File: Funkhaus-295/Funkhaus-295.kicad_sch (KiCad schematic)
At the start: 86 parts, among them SW1 SW_DPDT_x2, SW2 SW_Rotary3x4, SW3 SW_Rotary2x6, U1 TL074, U2 TL074, U3 TL074

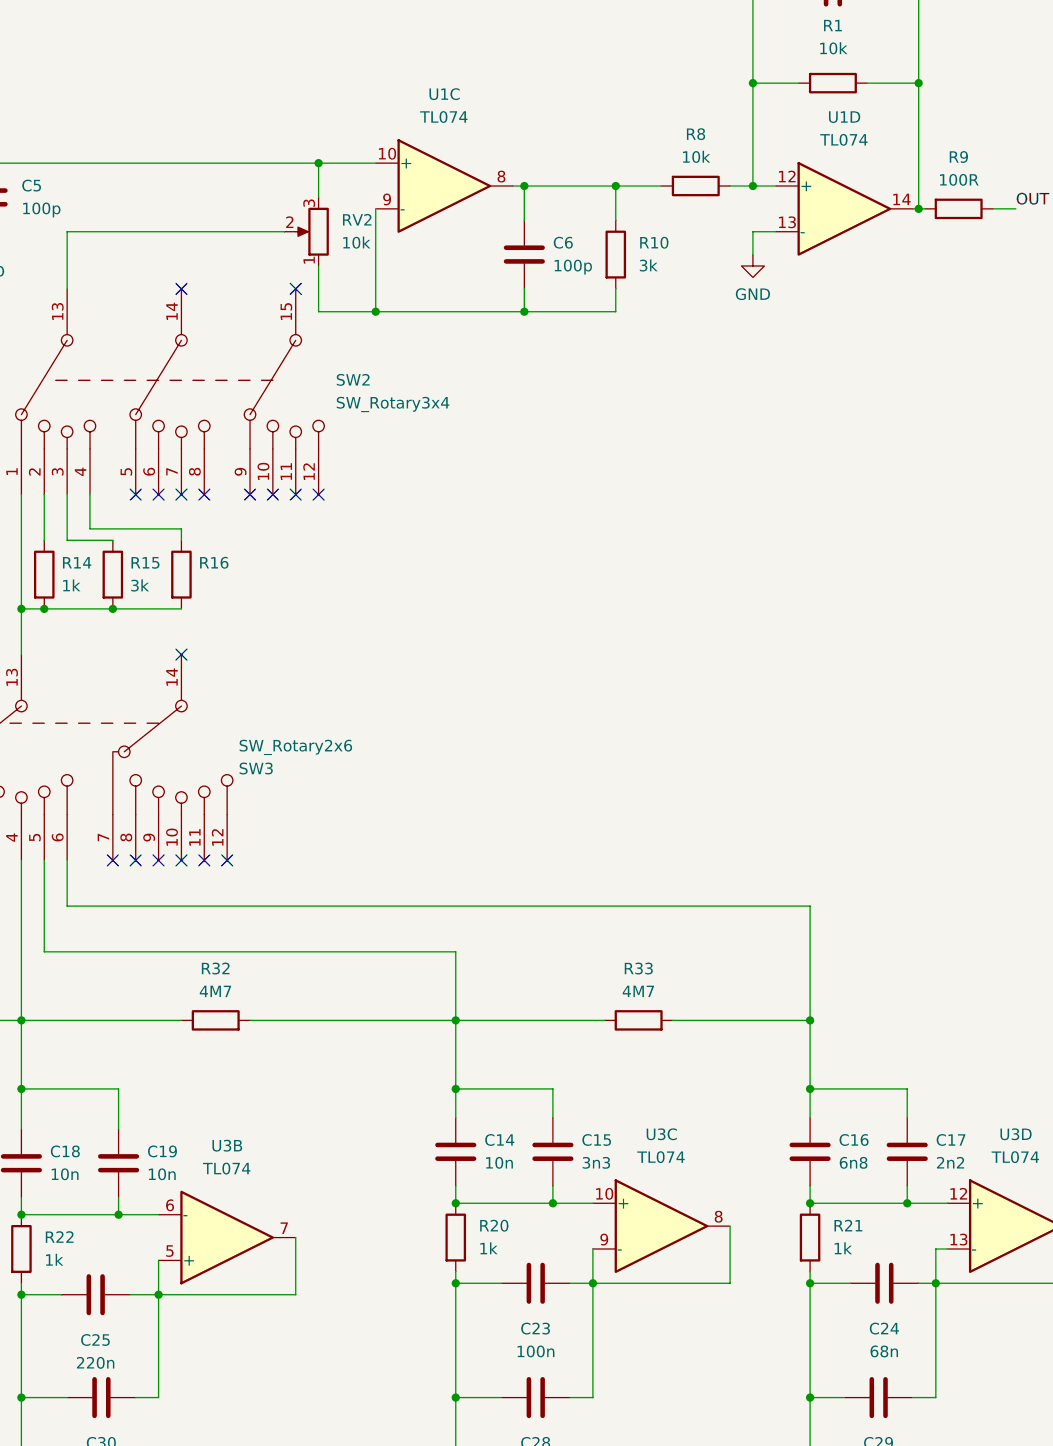
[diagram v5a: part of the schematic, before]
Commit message: Rev 05c
corrected the orientation of several opamps
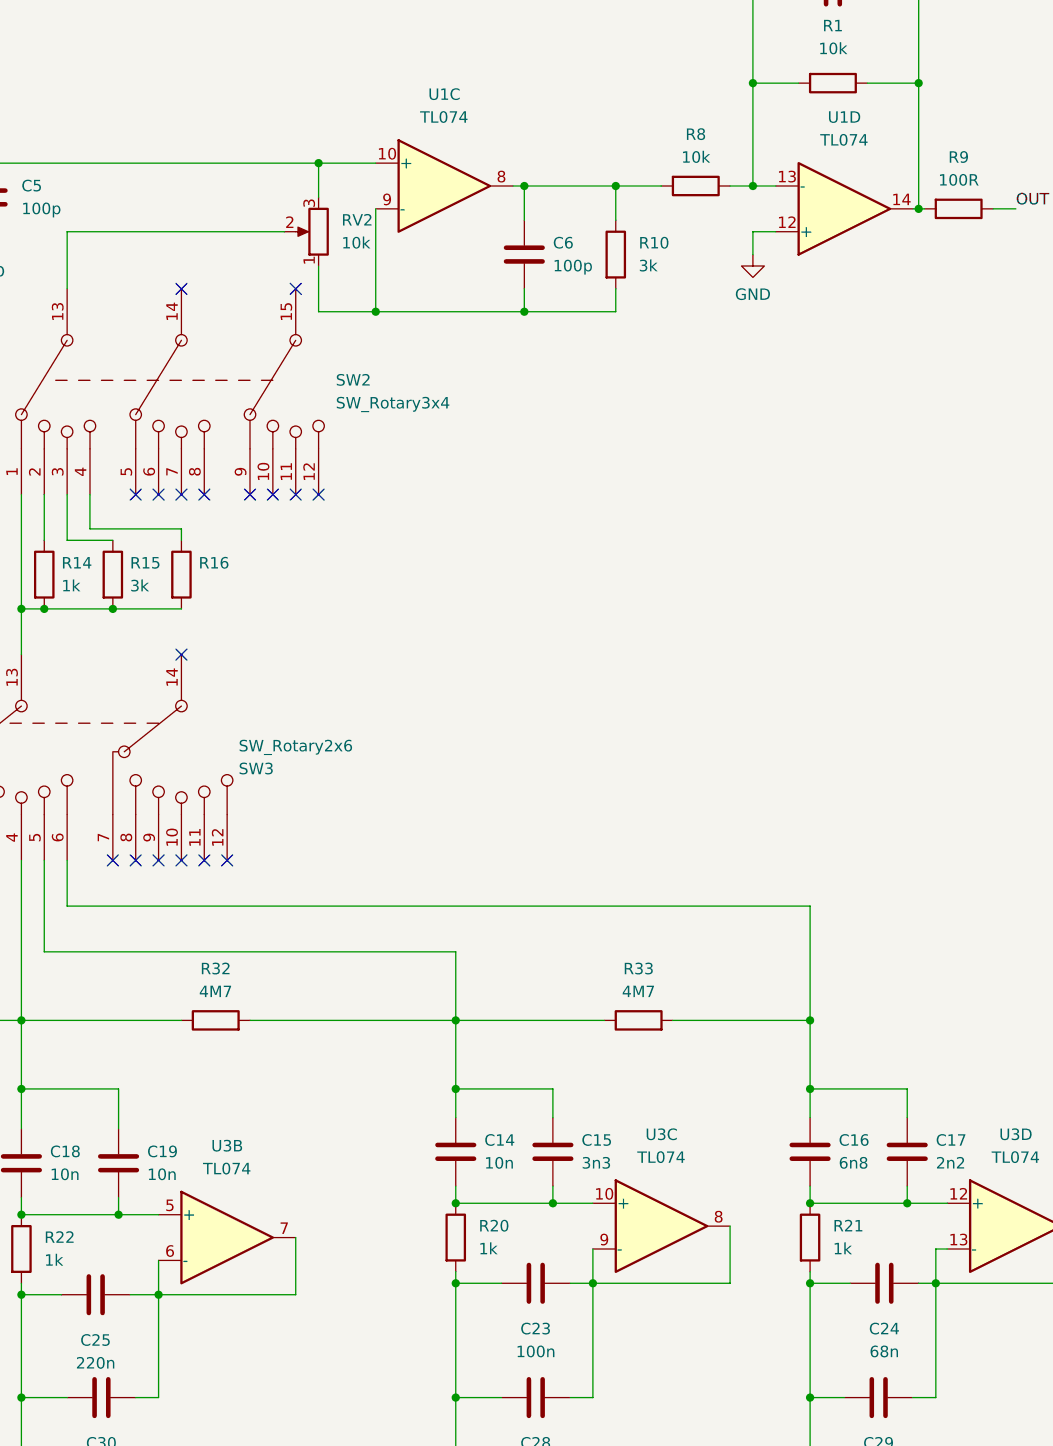
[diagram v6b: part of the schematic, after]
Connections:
- net GND: now also U1.12 (+); no longer U1.13 (-)
- net at C25.2, C30.2, U3.7: now also U3.6 (-); no longer U3.5 (+)
- net at C18.2, C19.2, R22.1: now also U3.5 (+); no longer U3.6 (-)
- net at C1.1, R1.2, R8.1: now also U1.13 (-); no longer U1.12 (+)
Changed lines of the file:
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@@
   (title_block
     (title "SIAM 295b")
-    (date "2022-08-07")
-    (rev "05a")
+    (date "2022-08-08")
+    (rev "05b")
     (company "Robert-André Vettel")
     (comment 1 "Siemens Inspired Audio Module")
@@
     (pin "2")
   )
-  (symbol (lib_id "Amplifier_Operational:TL074") (at 360.68 58.42 0) (unit 4)
+  (symbol (lib_id "Amplifier_Operational:TL074") (at 360.68 58.42 0) (mirror x) (unit 4)
     (in_bom yes) (on_board yes) (fields_autoplaced)
     (property "Reference" "U1" (id 0) (at 360.68 48.26 0))
     (property "Value" "TL074" (id 1) (at 360.68 50.8 0))
-    (property "Footprint" "" (id 2) (at 359.41 55.88 0)
-      (effects (font (size 1.27 1.27)) hide)
-    )
-    (property "Datasheet" "http://www.ti.com/lit/ds/symlink/tl071.pdf" (id 3) (at 361.95 53.34 0)
+    (property "Footprint" "" (id 2) (at 359.41 60.96 0)
+      (effects (font (size 1.27 1.27)) hide)
+    )
+    (property "Datasheet" "http://www.ti.com/lit/ds/symlink/tl071.pdf" (id 3) (at 361.95 63.5 0)
       (effects (font (size 1.27 1.27)) hide)
     )
@@
     (pin "1")
   )
-  (symbol (lib_id "Amplifier_Operational:TL074") (at 292.1 172.72 0) (mirror x) (unit 2)
+  (symbol (lib_id "Amplifier_Operational:TL074") (at 292.1 172.72 0) (unit 2)
     (in_bom yes) (on_board yes) (fields_autoplaced)
     (property "Reference" "U3" (id 0) (at 292.1 162.56 0))
     (property "Value" "TL074" (id 1) (at 292.1 165.1 0))
-    (property "Footprint" "" (id 2) (at 290.83 175.26 0)
-      (effects (font (size 1.27 1.27)) hide)
-    )
-    (property "Datasheet" "http://www.ti.com/lit/ds/symlink/tl071.pdf" (id 3) (at 293.37 177.8 0)
-      (effects (font (size 1.27 1.27)) hide)
-    )
+    (property "Footprint" "" (id 2) (at 290.83 170.18 0)
+      (effects (font (size 1.27 1.27)) hide)
+    )
+    (property "Datasheet" "http://www.ti.com/lit/ds/symlink/tl071.pdf" (id 3) (at 293.37 167.64 0)
+      (effects (font (size 1.27 1.27)) hide)
+    )

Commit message: housekeeping (Rev05C)
- corrected missing 10K resistor
- added output capacitor
- added annotations
- changed component numbering to make a little more sense
- added partial component footprints
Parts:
- added C34: 22u, Capacitor_THT:CP_Radial_D5.0mm_P2.50mm, symbol Device:C_Polarized
- added R32, R33, R34, R35, R36, R37, R38: 4M7, Resistor_THT:R_Axial_DIN0207_L6.3mm_D2.5mm_P2.54mm_Vertical, symbol Device:R
- C1: renamed from C8; footprint Capacitor_THT:C_Rect_L10.0mm_W3.0mm_P7.50mm_MKS4 -> (none)
- C2: renamed from C4; footprint Capacitor_THT:C_Rect_L10.0mm_W3.0mm_P7.50mm_MKS4 -> (none)
- C28: renamed from C5; footprint (none) -> Capacitor_THT:C_Disc_D5.0mm_W2.5mm_P5.00mm
- C29: renamed from C6; footprint (none) -> Capacitor_THT:C_Disc_D5.0mm_W2.5mm_P5.00mm
- C3: renamed from C9; footprint Capacitor_THT:C_Rect_L10.0mm_W3.0mm_P7.50mm_MKS4 -> (none)
- C31: renamed from C1; footprint (none) -> Capacitor_THT:C_Disc_D5.0mm_W2.5mm_P5.00mm
- C32: renamed from C2; footprint (none) -> Capacitor_THT:CP_Radial_D10.0mm_P5.00mm
- C33: renamed from C3; footprint (none) -> Capacitor_THT:CP_Radial_D5.0mm_P2.50mm
- C35: renamed from C31; footprint (none) -> Capacitor_THT:CP_Radial_D10.0mm_P5.00mm
- C36: renamed from C34; footprint (none) -> Capacitor_THT:CP_Radial_D10.0mm_P5.00mm
- C37: renamed from C32; footprint Capacitor_THT:C_Rect_L10.0mm_W3.0mm_P7.50mm_MKS4 -> Capacitor_THT:C_Disc_D5.0mm_W2.5mm_P5.00mm
- C38: renamed from C33; footprint Capacitor_THT:C_Rect_L10.0mm_W3.0mm_P7.50mm_MKS4 -> Capacitor_THT:C_Disc_D5.0mm_W2.5mm_P5.00mm
- C39: renamed from C35; footprint Capacitor_THT:C_Rect_L10.0mm_W3.0mm_P7.50mm_MKS4 -> Capacitor_THT:C_Disc_D5.0mm_W2.5mm_P5.00mm
- C40: renamed from C36; footprint Capacitor_THT:C_Rect_L10.0mm_W3.0mm_P7.50mm_MKS4 -> Capacitor_THT:C_Disc_D5.0mm_W2.5mm_P5.00mm
- C41: renamed from C37; footprint Capacitor_THT:C_Rect_L10.0mm_W3.0mm_P7.50mm_MKS4 -> Capacitor_THT:C_Disc_D5.0mm_W2.5mm_P5.00mm
- C42: renamed from C38; footprint Capacitor_THT:C_Rect_L10.0mm_W3.0mm_P7.50mm_MKS4 -> Capacitor_THT:C_Disc_D5.0mm_W2.5mm_P5.00mm
- R10: renamed from R34; footprint (none) -> Resistor_THT:R_Axial_DIN0207_L6.3mm_D2.5mm_P10.16mm_Horizontal
- R11: renamed from R17; footprint (none) -> Resistor_THT:R_Axial_DIN0207_L6.3mm_D2.5mm_P10.16mm_Horizontal
- R12: renamed from R24; footprint (none) -> Resistor_THT:R_Axial_DIN0207_L6.3mm_D2.5mm_P10.16mm_Horizontal
- R13: renamed from R35; footprint (none) -> Resistor_THT:R_Axial_DIN0207_L6.3mm_D2.5mm_P10.16mm_Horizontal
- R14: renamed from R36; footprint (none) -> Resistor_THT:R_Axial_DIN0207_L6.3mm_D2.5mm_P10.16mm_Horizontal
- R15: renamed from R18; footprint (none) -> Resistor_THT:R_Axial_DIN0207_L6.3mm_D2.5mm_P10.16mm_Horizontal
- R16: renamed from R23; footprint (none) -> Resistor_THT:R_Axial_DIN0207_L6.3mm_D2.5mm_P10.16mm_Horizontal
- R17: renamed from R7; footprint (none) -> Resistor_THT:R_Axial_DIN0207_L6.3mm_D2.5mm_P10.16mm_Horizontal
- R18: renamed from R22; footprint (none) -> Resistor_THT:R_Axial_DIN0207_L6.3mm_D2.5mm_P10.16mm_Horizontal
- R19: renamed from R28; footprint (none) -> Resistor_THT:R_Axial_DIN0207_L6.3mm_D2.5mm_P10.16mm_Horizontal
- R20: renamed from R14; footprint (none) -> Resistor_THT:R_Axial_DIN0207_L6.3mm_D2.5mm_P10.16mm_Horizontal
- R21: renamed from R15; footprint (none) -> Resistor_THT:R_Axial_DIN0207_L6.3mm_D2.5mm_P10.16mm_Horizontal
- R22: renamed from R16; value ~ -> 10k; footprint (none) -> Resistor_THT:R_Axial_DIN0207_L6.3mm_D2.5mm_P10.16mm_Horizontal
- R23: renamed from R20; footprint (none) -> Resistor_THT:R_Axial_DIN0207_L6.3mm_D2.5mm_P10.16mm_Horizontal
- R24: renamed from R26; footprint (none) -> Resistor_THT:R_Axial_DIN0207_L6.3mm_D2.5mm_P10.16mm_Horizontal
- R25: renamed from R10; footprint (none) -> Resistor_THT:R_Axial_DIN0207_L6.3mm_D2.5mm_P10.16mm_Horizontal
- R26: renamed from R21; footprint (none) -> Resistor_THT:R_Axial_DIN0207_L6.3mm_D2.5mm_P10.16mm_Horizontal
- R27: footprint (none) -> Resistor_THT:R_Axial_DIN0207_L6.3mm_D2.5mm_P10.16mm_Horizontal
- R28: renamed from R6; footprint (none) -> Resistor_THT:R_Axial_DIN0207_L6.3mm_D2.5mm_P10.16mm_Horizontal
- R29: renamed from R8; footprint (none) -> Resistor_THT:R_Axial_DIN0207_L6.3mm_D2.5mm_P10.16mm_Horizontal
- R30: renamed from R1; footprint (none) -> Resistor_THT:R_Axial_DIN0207_L6.3mm_D2.5mm_P10.16mm_Horizontal
- R31: renamed from R9; footprint (none) -> Resistor_THT:R_Axial_DIN0207_L6.3mm_D2.5mm_P10.16mm_Horizontal
- R39: renamed from R29; footprint (none) -> Resistor_THT:R_Axial_DIN0207_L6.3mm_D2.5mm_P2.54mm_Vertical
- R40: renamed from R30; footprint (none) -> Resistor_THT:R_Axial_DIN0207_L6.3mm_D2.5mm_P2.54mm_Vertical
- R41: renamed from R31; footprint (none) -> Resistor_THT:R_Axial_DIN0207_L6.3mm_D2.5mm_P2.54mm_Vertical
- R42: renamed from R32; footprint (none) -> Resistor_THT:R_Axial_DIN0207_L6.3mm_D2.5mm_P2.54mm_Vertical
- R43: renamed from R33; footprint (none) -> Resistor_THT:R_Axial_DIN0207_L6.3mm_D2.5mm_P2.54mm_Vertical
- R8: renamed from R19; footprint (none) -> Resistor_THT:R_Axial_DIN0207_L6.3mm_D2.5mm_P10.16mm_Horizontal
- R9: renamed from R25; footprint (none) -> Resistor_THT:R_Axial_DIN0207_L6.3mm_D2.5mm_P10.16mm_Horizontal
- RV1, RV2, RV3: footprint (none) -> Connector_PinHeader_2.54mm:PinHeader_1x03_P2.54mm_Horizontal
- SW1: footprint (none) -> Connector_PinHeader_2.54mm:PinHeader_2x03_P2.54mm_Horizontal
- SW2: footprint (none) -> Connector_PinHeader_2.54mm:PinHeader_1x05_P2.54mm_Horizontal
- SW3: footprint (none) -> Connector_PinHeader_2.54mm:PinHeader_1x07_P2.54mm_Horizontal
- U1, U2, U3: footprint (none) -> Package_DIP:DIP-14_W10.16mm
- renumbered C20 to C10, C26 to C11, C40 to C12, C41 to C13, C10 to C14, C21 to C15, C18 to C16, C25 to C17, C30 to C18, C14 to C20, C23 to C21, C28 to C22, C15 to C23, C16 to C24, C29 to C25, C24 to C26, C17 to C27, C7 to C30, C12 to C4, C22 to C5, C27 to C6, C13 to C7, C39 to C8, C11 to C9, R13 to R1, R4 to R2, R11 to R3, R2 to R4, R3 to R5, R5 to R6, R12 to R7
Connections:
- net at R2.2, SW1.1 (A), SW1.6 (C): now also R32.1, R35.2
- net at R6.1, SW1.3 (C), SW1.4 (A): now also R33.1, R34.2
- net at R21.1, SW2.3: now also R37.2, R38.1
- net at R20.2, R21.2, R22.2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: now also R36.1
- net at R20.1, SW2.2: now also R36.2, R37.1
- net at R22.1, SW2.4: now also R38.2
- net at R5.2, SW1.5 (B): now also R34.1, R35.1
- net at C29.1, R25.1, U1.8: now also C34.1; no longer R29.2
- net at RV1.1, SW1.2 (B): now also R32.2, R33.2
- new net: C34.2, R29.2
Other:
- note added: "0.7 kHz"
- note added: "1.0 kHz"
- note added: "1.5 kHz"
- note added: "2.3 kHz"
- note added: "24kHz Low-pass filter"
- note added: "3.5 kHz"
- note added: "5.6 kHz"
- note added: "Gain-mod 8dB = - 6dB = 1k 4dB = 3k 2dB = 10k"
- note added: "High & Low shelf"
- note added: "Input buffer"
- note added: "Mid band"
- note added: "Output buffer"
- note removed: "0,7 kHz = 72n7 / 727n (680 + 47) 1,0 kHz = 47n / 538n (470 + 68) 1.5 kHz = 33n / 330n 2.3 kHz = 20n / 235n (220+15) 3.5 kHz = 13n3 / 147n 5.6 kHz = 9n / 90n (68 + 22)"
- note removed: "Q-Mod"
- moved on the sheet: C1, C10, C11, C12, C13, C14, C15, C16, C17, C18, C19, C2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

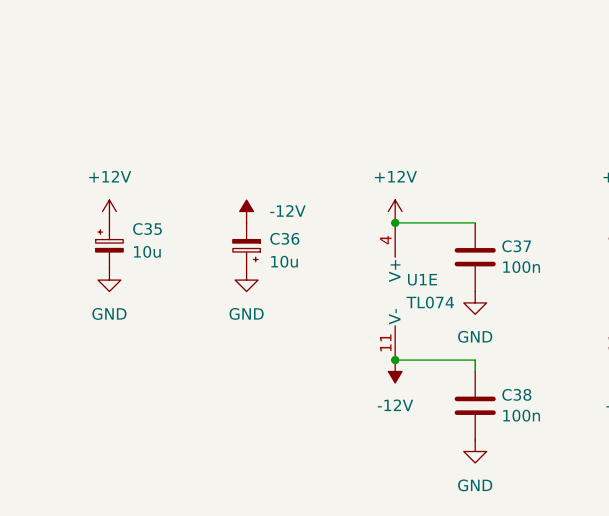
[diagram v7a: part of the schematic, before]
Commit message: fixed C35/C36 Symbol
fixed C35/C36 Symbol
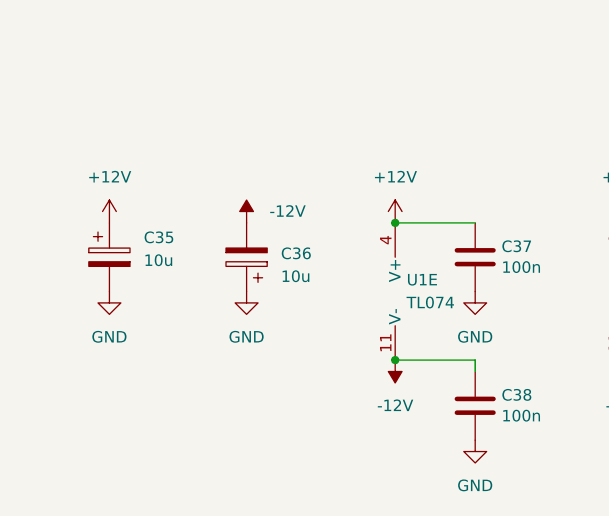
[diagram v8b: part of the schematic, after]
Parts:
- removed C35, C36: 10u, Capacitor_THT:CP_Radial_D10.0mm_P5.00mm, symbol Device:C_Polarized_Small
- added C35, C36: 10u, Capacitor_THT:CP_Radial_D10.0mm_P5.00mm, symbol Device:C_Polarized
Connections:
- net +12V: now also C35.1
- net -12V: now also C36.2
- net GND: now also C35.2, C36.1
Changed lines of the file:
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@@
-    (pin "2")
-  )
-  (symbol (lib_id "Device:C_Polarized_Small") (at 41.91 247.65 180) (unit 1)
-    (in_bom yes) (on_board yes) (fields_autoplaced)
-    (property "Reference" "C36" (id 0) (at 44.45 246.926 0)
-      (effects (font (size 1.27 1.27)) (justify right))
-    )
-    (property "Value" "10u" (id 1) (at 44.45 249.466 0)
-      (effects (font (size 1.27 1.27)) (justify right))
-    )
-    (property "Footprint" "Capacitor_THT:CP_Radial_D10.0mm_P5.00mm" (id 2) (at 41.91 247.65 0)
-      (effects (font (size 1.27 1.27)) hide)
-    )
-    (property "Datasheet" "~" (id 3) (at 41.91 247.65 0)
-      (effects (font (size 1.27 1.27)) hide)
-    )
-    (pin "1")
     (pin "2")
   )
@@
     (pin "4")
   )
-  (symbol (lib_id "power:GND") (at 41.91 250.19 0) (unit 1)
-    (in_bom yes) (on_board yes) (fields_autoplaced)
-    (property "Reference" "#PWR014" (id 0) (at 41.91 256.54 0)
-      (effects (font (size 1.27 1.27)) hide)
-    )
-    (property "Value" "GND" (id 1) (at 41.91 255.27 0))
-    (property "Footprint" "" (id 2) (at 41.91 250.19 0)
-      (effects (font (size 1.27 1.27)) hide)
-    )
-    (property "Datasheet" "" (id 3) (at 41.91 250.19 0)
+  (symbol (lib_id "power:GND") (at 41.91 252.73 0) (unit 1)
+    (in_bom yes) (on_board yes) (fields_autoplaced)
+    (property "Reference" "#PWR014" (id 0) (at 41.91 259.08 0)
+      (effects (font (size 1.27 1.27)) hide)
+    )
+    (property "Value" "GND" (id 1) (at 41.91 257.81 0))
+    (property "Footprint" "" (id 2) (at 41.91 252.73 0)
+      (effects (font (size 1.27 1.27)) hide)
+    )
+    (property "Datasheet" "" (id 3) (at 41.91 252.73 0)
       (effects (font (size 1.27 1.27)) hide)
     )
@@
     (pin "2")
   )
-  (symbol (lib_id "Device:C_Polarized_Small") (at 26.67 247.65 0) (unit 1)
-    (in_bom yes) (on_board yes) (fields_autoplaced)
-    (property "Reference" "C35" (id 0) (at 29.21 245.8338 0)
-      (effects (font (size 1.27 1.27)) (justify left))
-    )
-    (property "Value" "10u" (id 1) (at 29.21 248.3738 0)
-      (effects (font (size 1.27 1.27)) (justify left))
-    )
-    (property "Footprint" "Capacitor_THT:CP_Radial_D10.0mm_P5.00mm" (id 2) (at 26.67 247.65 0)
-      (effects (font (size 1.27 1.27)) hide)
-    )
-    (property "Datasheet" "~" (id 3) (at 26.67 247.65 0)
-      (effects (font (size 1.27 1.27)) hide)
-    )
-    (pin "1")
-    (pin "2")
-  )
   (symbol (lib_id "Device:R") (at 127 41.91 90) (unit 1)
     (in_bom yes) (on_board yes) (fields_autoplaced)
@@
     (pin "2")
   )
-  (symbol (lib_id "power:GND") (at 26.67 250.19 0) (unit 1)
-    (in_bom yes) (on_board yes) (fields_autoplaced)
-    (property "Reference" "#PWR08" (id 0) (at 26.67 256.54 0)
-      (effects (font (size 1.27 1.27)) hide)
-    )
-    (property "Value" "GND" (id 1) (at 26.67 255.27 0))
-    (property "Footprint" "" (id 2) (at 26.67 250.19 0)
-      (effects (font (size 1.27 1.27)) hide)
-    )
-    (property "Datasheet" "" (id 3) (at 26.67 250.19 0)
+  (symbol (lib_id "power:GND") (at 26.67 252.73 0) (unit 1)
+    (in_bom yes) (on_board yes) (fields_autoplaced)
+    (property "Reference" "#PWR08" (id 0) (at 26.67 259.08 0)
+      (effects (font (size 1.27 1.27)) hide)
+    )
+    (property "Value" "GND" (id 1) (at 26.67 257.81 0))
+    (property "Footprint" "" (id 2) (at 26.67 252.73 0)
+      (effects (font (size 1.27 1.27)) hide)
+    )
+    (property "Datasheet" "" (id 3) (at 26.67 252.73 0)
       (effects (font (size 1.27 1.27)) hide)
     )
@@
     (pin "2")
   )
+  (symbol (lib_id "Device:C_Polarized") (at 26.67 248.92 0) (unit 1)
+    (in_bom yes) (on_board yes) (fields_autoplaced)
+    (property "Reference" "C35" (id 0) (at 30.48 246.7609 0)
+      (effects (font (size 1.27 1.27)) (justify left))
+    )
+    (property "Value" "10u" (id 1) (at 30.48 249.3009 0)
+      (effects (font (size 1.27 1.27)) (justify left))
+    )
+    (property "Footprint" "Capacitor_THT:CP_Radial_D10.0mm_P5.00mm" (id 2) (at 27.6352 252.73 0)
+      (effects (font (size 1.27 1.27)) hide)
+    )
+    (property "Datasheet" "~" (id 3) (at 26.67 248.92 0)
+      (effects (font (size 1.27 1.27)) hide)
+    )
+    (pin "1")
+    (pin "2")
+  )
   (symbol (lib_id "Amplifier_Operational:TL074") (at 215.9 193.04 0) (unit 4)
     (in_bom yes) (on_board yes) (fields_autoplaced)
@@
     (pin "4")
   )
+  (symbol (lib_id "Device:C_Polarized") (at 41.91 248.92 180) (unit 1)
+    (in_bom yes) (on_board yes) (fields_autoplaced)
+    (property "Reference" "C36" (id 0) (at 45.72 248.5389 0)
+      (effects (font (size 1.27 1.27)) (justify right))
+    )
+    (property "Value" "10u" (id 1) (at 45.72 251.0789 0)
+      (effects (font (size 1.27 1.27)) (justify right))
+    )
+    (property "Footprint" "Capacitor_THT:CP_Radial_D10.0mm_P5.00mm" (id 2) (at 40.9448 245.11 0)
+      (effects (font (size 1.27 1.27)) hide)
+    )
+    (property "Datasheet" "~" (id 3) (at 41.91 248.92 0)
+      (effects (font (size 1.27 1.27)) hide)
+    )
+    (pin "1")
+    (pin "2")
+  )
   (symbol (lib_id "Device:C") (at 364.49 213.36 90) (unit 1)
     (in_bom yes) (on_board yes)
@@
       (reference "C34") (unit 1) (value "22u") (footprint "Capacitor_THT:CP_Radial_D5.0mm_P2.50mm")
     )
-    (path "/2f467b0c-a8c5-40a0-91b6-8e4cc93cfc8d"
+    (path "/777cc4ba-2bfe-4519-9fe1-08dd087fa9d1"
       (reference "C35") (unit 1) (value "10u") (footprint "Capacitor_THT:CP_Radial_D10.0mm_P5.00mm")
     )
-    (path "/119ff35c-8d95-41d3-a7fb-f5ee71aa6b30"
+    (path "/996cf147-4756-462c-a0bf-5d6ad287bce9"
       (reference "C36") (unit 1) (value "10u") (footprint "Capacitor_THT:CP_Radial_D10.0mm_P5.00mm")
     )
